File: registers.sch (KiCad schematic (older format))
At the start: 4 parts

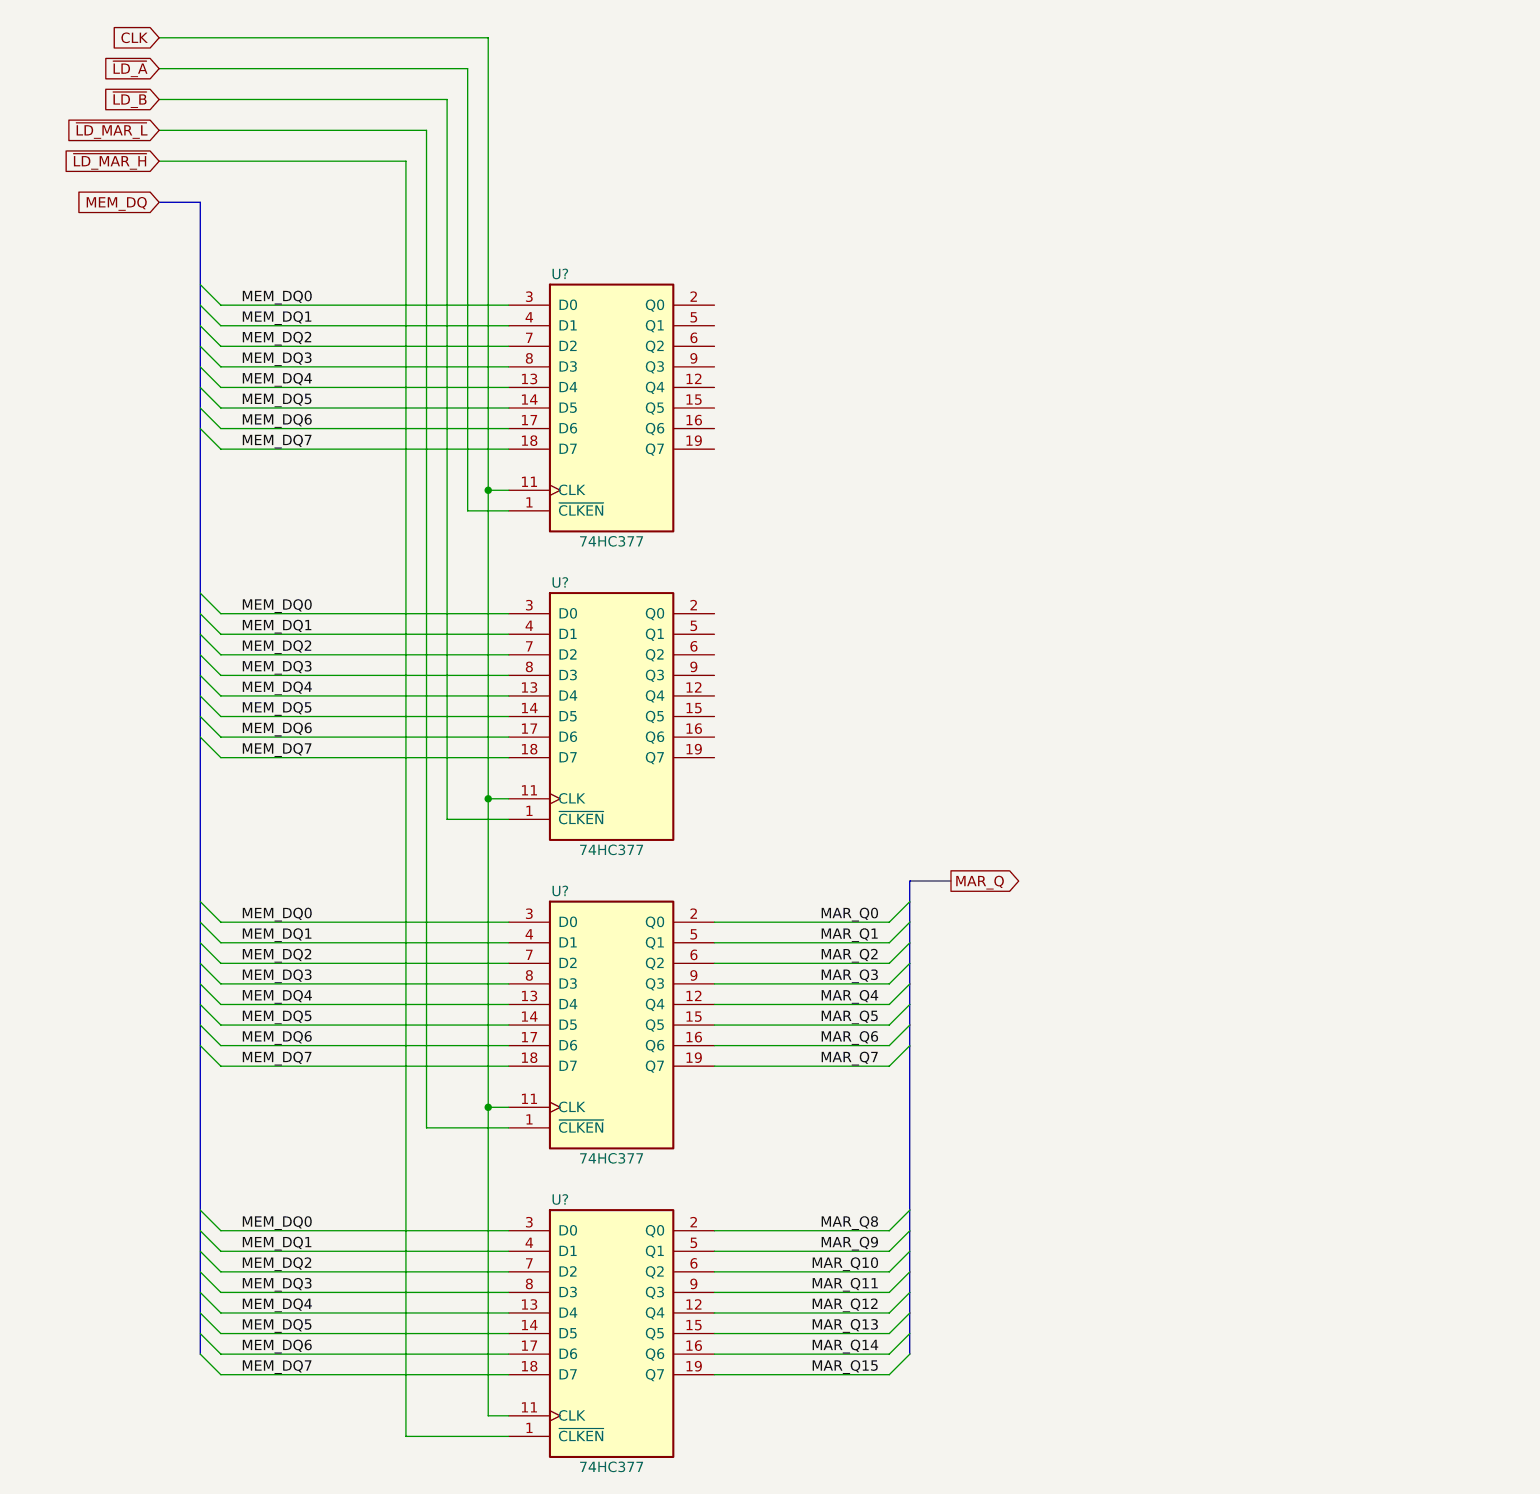
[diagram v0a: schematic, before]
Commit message: split alu regs complete
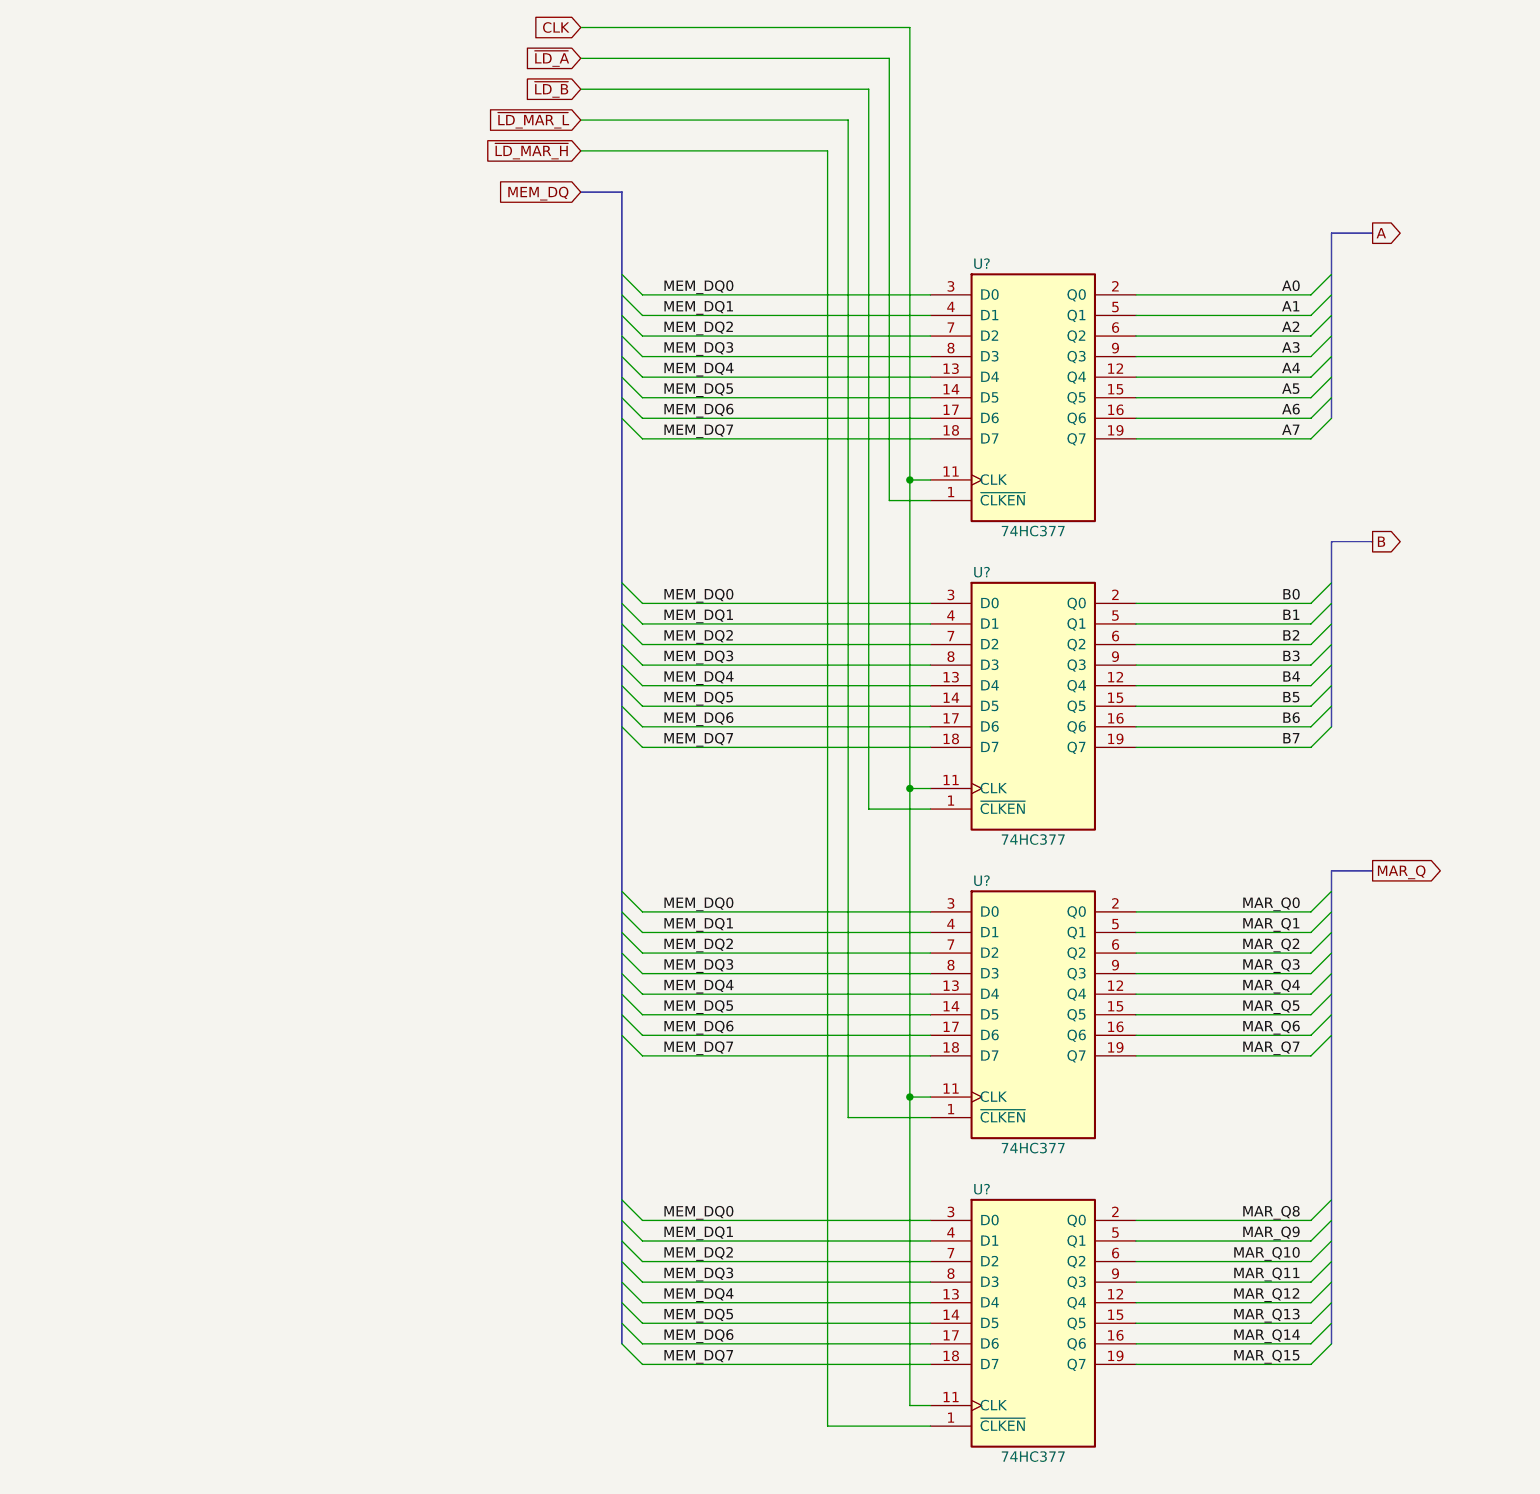
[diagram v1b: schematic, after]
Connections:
- net A4: now reaches U?.12 (Q4)
- net A5: now reaches U?.15 (Q5)
- net A6: now reaches U?.16 (Q6)
- net A7: now reaches U?.19 (Q7)
- net A0: now reaches U?.2 (Q0)
- net A1: now reaches U?.5 (Q1)
- net A2: now reaches U?.6 (Q2)
- net A3: now reaches U?.9 (Q3)
- net B4: now reaches U?.12 (Q4)
- net B5: now reaches U?.15 (Q5)
- net B6: now reaches U?.16 (Q6)
- net B7: now reaches U?.19 (Q7)
- net B0: now reaches U?.2 (Q0)
- net B1: now reaches U?.5 (Q1)
- net B2: now reaches U?.6 (Q2)
- net B3: now reaches U?.9 (Q3)
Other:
- moved on the sheet: U?

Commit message: done for the night passing drc
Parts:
- gave numbers to parts that had none: 4
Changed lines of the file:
@@
 $Descr USLedger 17000 11000
 encoding utf-8
-Sheet 6 6
+Sheet 5 7
 Title ""
 Date ""
@@
 	9350 8500 10200 8500
 Text GLabel 6650 2800 0    50   Input ~ 0
-MEM_DQ
+MEM_DQ[0..7]
 Text Label 7050 3300 0    50   ~ 0
 MEM_DQ0
@@
 AR Path="/5C4D6ED1/5CBC6F47" Ref="U?"  Part="1"
 AR Path="/5CB820A3/5CBC6F47" Ref="U?"  Part="1"
-AR Path="/5CBC693B/5CBC6F47" Ref="U?"  Part="1"
-F 0 "U?" H 8600 4450 50  0000 C CNN
+AR Path="/5CBC693B/5CBC6F47" Ref="U18"  Part="1"
+F 0 "U18" H 8600 4450 50  0000 C CNN
 F 1 "74HC377" H 8850 3150 50  0000 C CNN
 F 2 "" H 8850 3800 50  0001 C CNN
@@
 AR Path="/5C4D6ED1/5CBC6F4E" Ref="U?"  Part="1"
 AR Path="/5CB820A3/5CBC6F4E" Ref="U?"  Part="1"
-AR Path="/5CBC693B/5CBC6F4E" Ref="U?"  Part="1"
-F 0 "U?" H 8600 5950 50  0000 C CNN
+AR Path="/5CBC693B/5CBC6F4E" Ref="U19"  Part="1"
+F 0 "U19" H 8600 5950 50  0000 C CNN
 F 1 "74HC377" H 8850 4650 50  0000 C CNN
 F 2 "" H 8850 5300 50  0001 C CNN
@@
 AR Path="/5C4D6ED1/5CBC6F55" Ref="U?"  Part="1"
 AR Path="/5CB820A3/5CBC6F55" Ref="U?"  Part="1"
-AR Path="/5CBC693B/5CBC6F55" Ref="U?"  Part="1"
-F 0 "U?" H 8600 7450 50  0000 C CNN
+AR Path="/5CBC693B/5CBC6F55" Ref="U20"  Part="1"
+F 0 "U20" H 8600 7450 50  0000 C CNN
 F 1 "74HC377" H 8850 6150 50  0000 C CNN
 F 2 "" H 8850 6800 50  0001 C CNN
@@
 AR Path="/5C4D6ED1/5CBC6F5C" Ref="U?"  Part="1"
 AR Path="/5CB820A3/5CBC6F5C" Ref="U?"  Part="1"
-AR Path="/5CBC693B/5CBC6F5C" Ref="U?"  Part="1"
-F 0 "U?" H 8600 8950 50  0000 C CNN
+AR Path="/5CBC693B/5CBC6F5C" Ref="U21"  Part="1"
+F 0 "U21" H 8600 8950 50  0000 C CNN
 F 1 "74HC377" H 8850 7650 50  0000 C CNN
 F 2 "" H 8850 8300 50  0001 C CNN
@@
 CLK
 Text GLabel 10500 6100 2    50   Output ~ 0
-MAR_Q
+MAR_Q[0..15]
 Connection ~ 8250 7200
 Wire Wire Line
@@
 	10300 3000 10500 3000
 Text GLabel 10500 3000 2    50   Output ~ 0
-A
+A[0..7]
 Text GLabel 10500 4500 2    50   Output ~ 0
-B
+B[0..7]
 Text Label 10150 3300 2    50   ~ 0
 A0

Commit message: calling it a night
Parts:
- U18, U19, U20, U21: footprint (none) -> Package_DIP:DIP-20_W7.62mm
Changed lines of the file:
@@
 F 0 "U18" H 8600 4450 50  0000 C CNN
 F 1 "74HC377" H 8850 3150 50  0000 C CNN
-F 2 "" H 8850 3800 50  0001 C CNN
+F 2 "Package_DIP:DIP-20_W7.62mm" H 8850 3800 50  0001 C CNN
 F 3 "http://www.ti.com/lit/gpn/sn74LS377" H 8850 3800 50  0001 C CNN
 	1    8850 3800
@@
 F 0 "U19" H 8600 5950 50  0000 C CNN
 F 1 "74HC377" H 8850 4650 50  0000 C CNN
-F 2 "" H 8850 5300 50  0001 C CNN
+F 2 "Package_DIP:DIP-20_W7.62mm" H 8850 5300 50  0001 C CNN
 F 3 "http://www.ti.com/lit/gpn/sn74LS377" H 8850 5300 50  0001 C CNN
 	1    8850 5300
@@
 F 0 "U20" H 8600 7450 50  0000 C CNN
 F 1 "74HC377" H 8850 6150 50  0000 C CNN
-F 2 "" H 8850 6800 50  0001 C CNN
+F 2 "Package_DIP:DIP-20_W7.62mm" H 8850 6800 50  0001 C CNN
 F 3 "http://www.ti.com/lit/gpn/sn74LS377" H 8850 6800 50  0001 C CNN
 	1    8850 6800
@@
 F 0 "U21" H 8600 8950 50  0000 C CNN
 F 1 "74HC377" H 8850 7650 50  0000 C CNN
-F 2 "" H 8850 8300 50  0001 C CNN
+F 2 "Package_DIP:DIP-20_W7.62mm" H 8850 8300 50  0001 C CNN
 F 3 "http://www.ti.com/lit/gpn/sn74LS377" H 8850 8300 50  0001 C CNN
 	1    8850 8300
